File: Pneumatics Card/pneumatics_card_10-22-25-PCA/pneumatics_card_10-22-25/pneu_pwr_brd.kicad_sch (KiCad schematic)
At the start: 40 parts, among them J1 2X1, J2 2X1, J3 2X1, J4 2X1, J5 2X1, J6 2X1, Q1 BSS138, Q2 BSS138, Q3 FQP30N06L, Q4 FQP30N06L, Q5 FQP30N06L, Q6 FQP30N06L, Q7 IRF4905SPbF, U1 L7805, U2 LD1117V33, U3 PCA9685

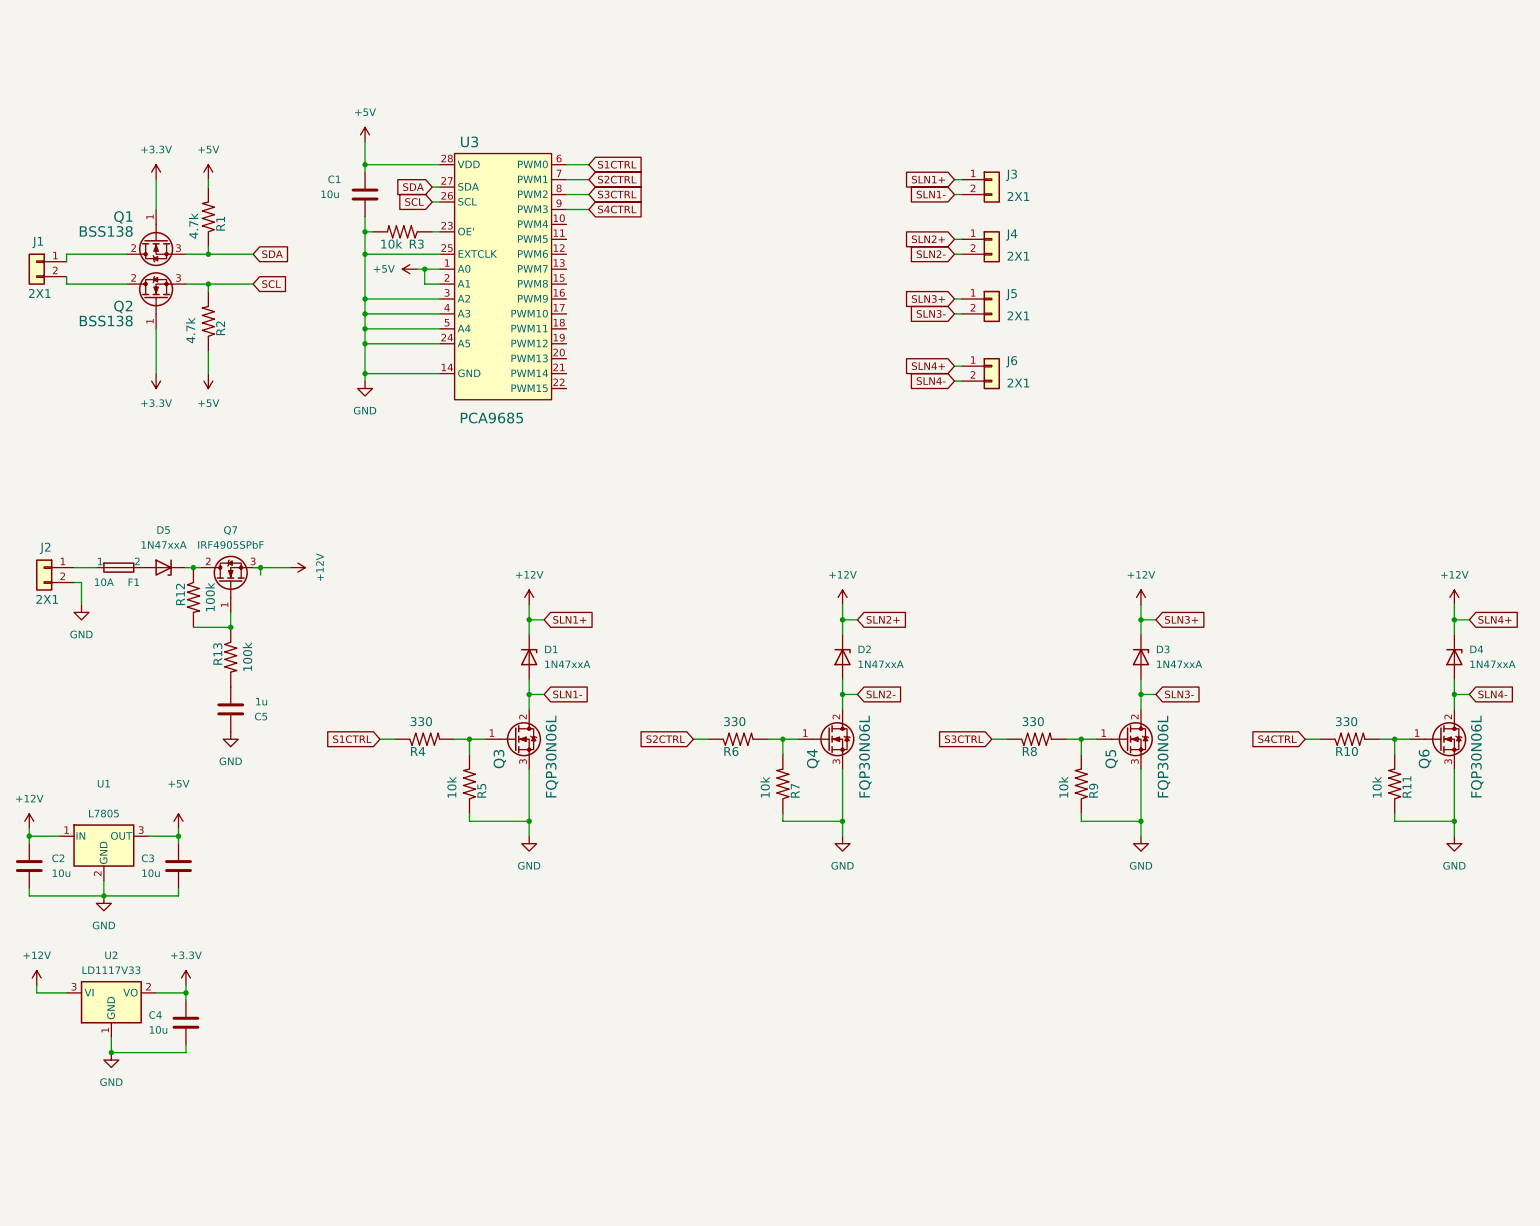
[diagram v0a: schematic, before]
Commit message: added inrush protection to old pneumatics board
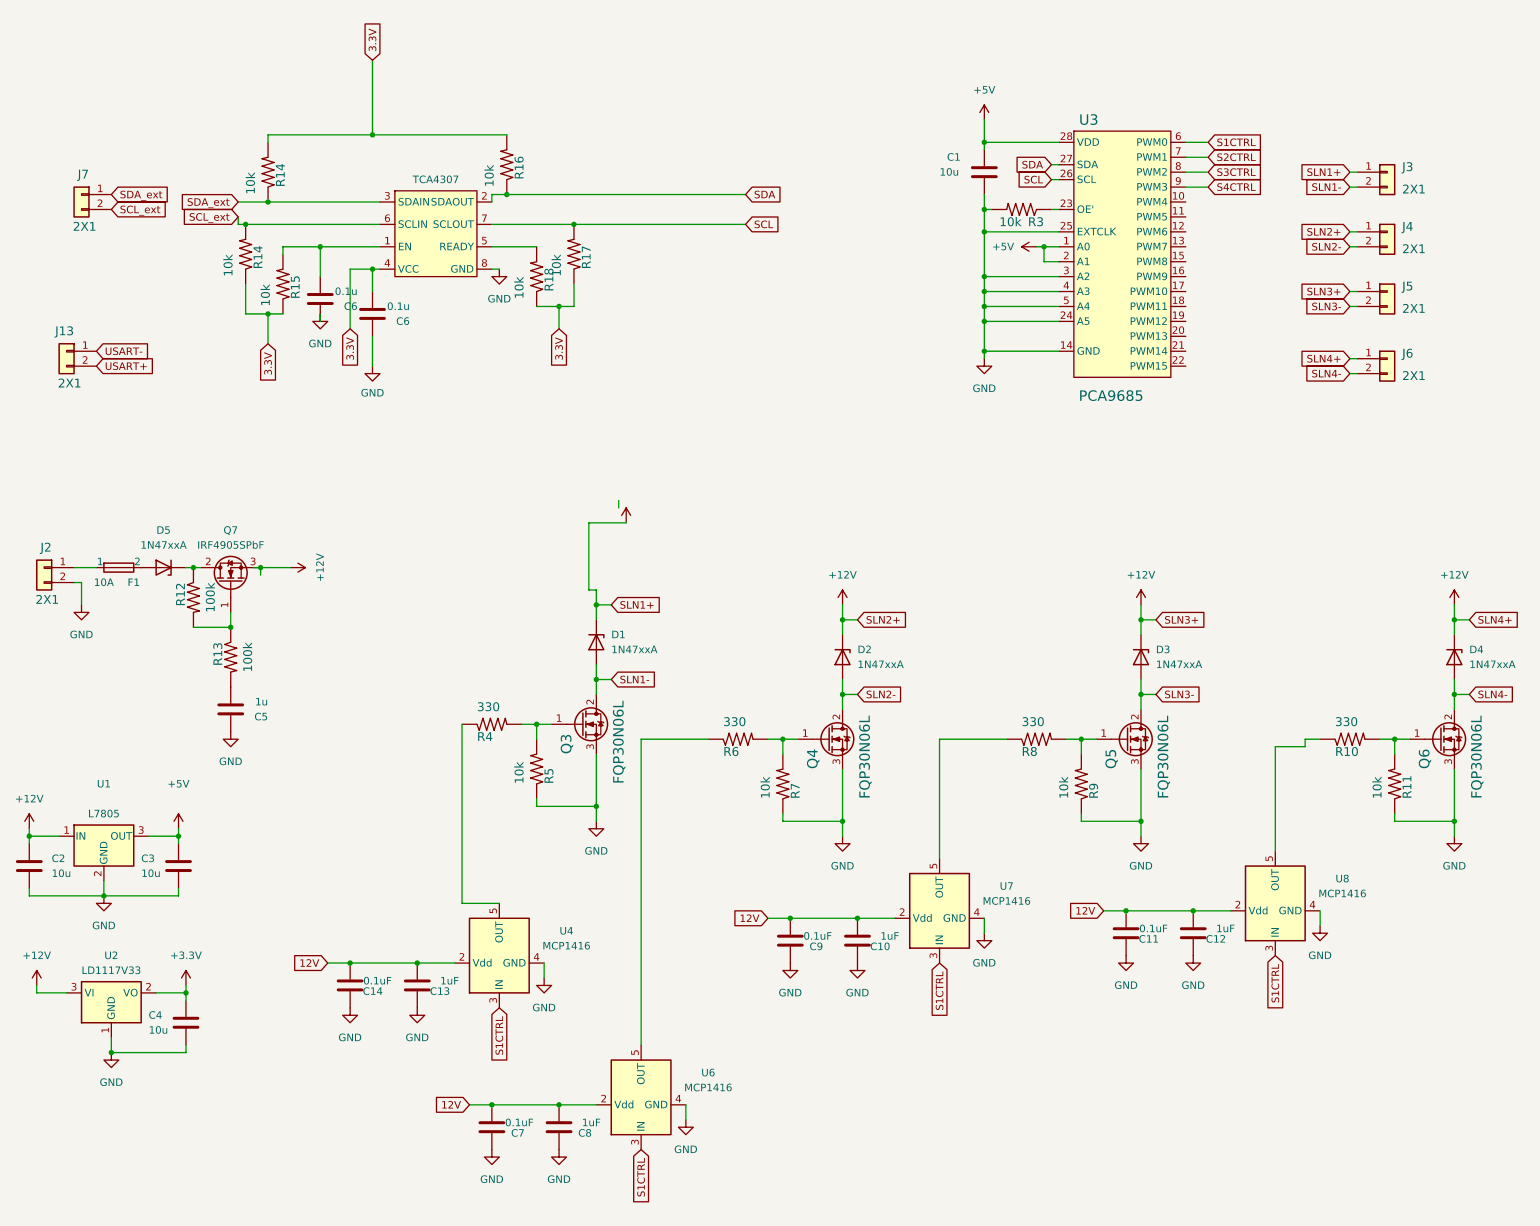
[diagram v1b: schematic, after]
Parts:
- removed J1: 2X1, Connector_JST:JST_PH_B2B-PH-K_1x02_P2.00mm_Vertical, symbol Connector_Generic:Conn_01x02
- removed Q1, Q2: BSS138, Package_TO_SOT_SMD:SOT-23_Handsoldering, symbol Transistor_FET:IRLZ34N
- removed R1, R2: 4.7k, Resistor_SMD:R_0805_2012Metric_Pad1.20x1.40mm_HandSolder, symbol PowerboardRev5-eagle-import:R-US_R0805
- added C10, C12, C13, C8: 1uF, Capacitor_SMD:C_0402_1005Metric, symbol Device:C
- added C11, C14, C7, C9: 0.1uF, Capacitor_SMD:C_0402_1005Metric, symbol Device:C
- added C6 (x2): 0.1u, Capacitor_SMD:C_0603_1608Metric, symbol Device:C
- added J13, J7: 2X1, Connector_JST:JST_PH_B2B-PH-K_1x02_P2.00mm_Vertical, symbol Connector_Generic:Conn_01x02
- added R14 (x2), R15, R16, R17, R18: 10k, Resistor_SMD:R_0603_1608Metric, symbol PowerboardRev5-eagle-import:R-US_R0805
- added U4, U6, U7, U8: MCP1416, Package_TO_SOT_SMD:SOT-23-5, symbol Driver_FET:MCP1416
- added U5: TCA4307, custom_components:SOIC8_DGK_TEX, symbol I2C_Buffer:T_1
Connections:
- net GND: now also C10.1, C11.1, C12.1, C13.1, C14.1, C6.1, C6.1, C7.1, C8.1, C9.1, U4.4 (GND), U5.8 (GND), U6.4 (GND), U7.4 (GND), U8.4 (GND)
- net S1CTRL: now also U4.3 (IN), U6.3 (IN), U7.3 (IN), U8.3 (IN); no longer R4.1
- net S2CTRL: no longer R6.1
- net S3CTRL: no longer R8.1
- net S4CTRL: no longer R10.1
- net SCL: now also R17.2, U5.7 (SCLOUT)
- net SDA: now also R16.1, U5.2 (SDAOUT)
- new net: R4.1, U4.5 (OUT)
- new net: R8.1, U7.5 (OUT)
- new net: R18.2, U5.5 (READY)
- new net: C6.2, R15.2, U5.1 (EN)
- new net: R10.1, U8.5 (OUT)
- new net: R6.1, U6.5 (OUT)
- new net 12V: C10.2, C11.2, C12.2, C13.2, C14.2, C7.2, C8.2, C9.2, U4.2 (Vdd), U6.2 (Vdd), U7.2 (Vdd), U8.2 (Vdd)
- new net 3.3V: C6.2, R14.1, R14.2, R15.1, R16.2, R17.1, R18.1, U5.4 (VCC)
- new net SCL_ext: J7.2 (Pin_2), R14.2, U5.6 (SCLIN)
- new net SDA_ext: J7.1 (Pin_1), R14.1, U5.3 (SDAIN)
- new net USART+: J13.2 (Pin_2)
- new net USART-: J13.1 (Pin_1)
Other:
- moved on the sheet: C1, D1, J3, J4, J5, J6, Q3, R3, R4, R5, U3

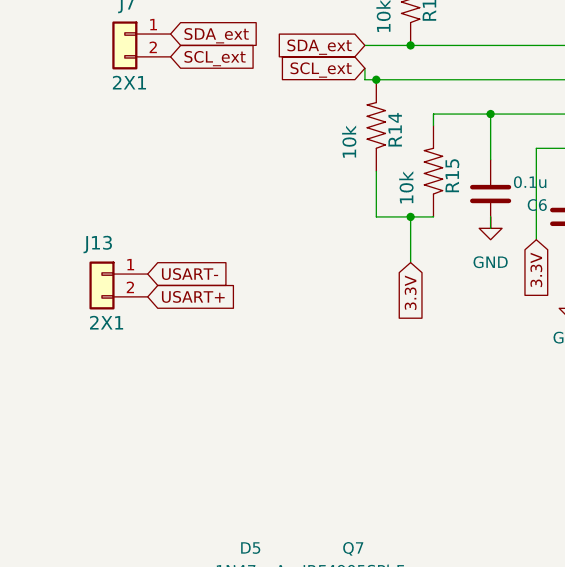
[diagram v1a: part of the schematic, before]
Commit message: fixed footprint for old pneumatics card
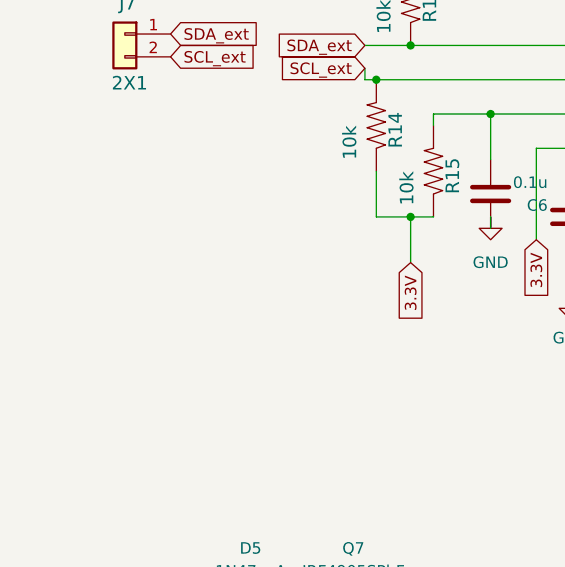
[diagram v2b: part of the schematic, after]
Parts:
- removed J13: 2X1, Connector_JST:JST_PH_B2B-PH-K_1x02_P2.00mm_Vertical, symbol Connector_Generic:Conn_01x02
- U5: footprint custom_components:SOIC8_DGK_TEX -> TCA4307:SOP65P490X110-8N
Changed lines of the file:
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@@
 		)
 	)
-	(global_label "USART-"
-		(shape input)
-		(at 35.56 58.42 0)
-		(fields_autoplaced yes)
-		(effects
-			(font
-				(size 1.27 1.27)
-			)
-			(justify left)
-		)
-		(property "Intersheetrefs" "${INTERSHEET_REFS}"
-			(at 45.9838 58.42 0)
-			(effects
-				(font
-					(size 1.27 1.27)
-				)
-				(justify left)
-				(hide yes)
-			)
-		)
-	)
 	(global_label "SLN1+"
 		(shape input)
@@
 		)
 	)
-	(global_label "USART+"
-		(shape input)
-		(at 35.56 60.96 0)
-		(fields_autoplaced yes)
-		(effects
-			(font
-				(size 1.27 1.27)
-			)
-			(justify left)
-		)
-		(property "Intersheetrefs" "${INTERSHEET_REFS}"
-			(at 45.9838 60.96 0)
-			(effects
-				(font
-					(size 1.27 1.27)
-				)
-				(justify left)
-				(hide yes)
-			)
-		)
-	)
 	(global_label "SLN3+"
 		(shape input)
@@
 	)
 	(symbol
-		(lib_id "Connector_Generic:Conn_01x02")
-		(at 30.48 58.42 0)
-		(mirror y)
-		(unit 1)
-		(exclude_from_sim no)
-		(in_bom yes)
-		(on_board yes)
-		(dnp no)
-		(property "Reference" "J13"
-			(at 31.75 55.88 0)
-			(effects
-				(font
-					(size 1.4986 1.4986)
-				)
-				(justify left bottom)
-			)
-		)
-		(property "Value" "2X1"
-			(at 33.02 64.77 0)
-			(effects
-				(font
-					(size 1.4986 1.4986)
-				)
-				(justify left bottom)
-			)
-		)
-		(property "Footprint" "Connector_JST:JST_PH_B2B-PH-K_1x02_P2.00mm_Vertical"
-			(at 30.48 58.42 0)
-			(effects
-				(font
-					(size 1.27 1.27)
-				)
-				(hide yes)
-			)
-		)
-		(property "Datasheet" "~"
-			(at 30.48 58.42 0)
-			(effects
-				(font
-					(size 1.27 1.27)
-				)
-				(hide yes)
-			)
-		)
-		(property "Description" ""
-			(at 30.48 58.42 0)
-			(effects
-				(font
-					(size 1.27 1.27)
-				)
-			)
-		)
-		(pin "1"
-		)
-		(pin "2"
-		)
-		(instances
-			(project "pneu_pwr_brd"
-				(path "/c299c6f2-212e-472c-8577-e7ed124513dd"
-					(reference "J13")
-					(unit 1)
-				)
-			)
-		)
-	)
-	(symbol
 		(lib_id "PowerboardRev5-eagle-import:R-US_R0805")
 		(at 67.31 46.99 270)
@@
 			)
 		)
-		(property "Footprint" "custom_components:SOIC8_DGK_TEX"
+		(property "Footprint" "TCA4307:SOP65P490X110-8N"
 			(at 96.52 35.56 0)
 			(effects

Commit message: tesitng
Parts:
- renumbered R15 to R155
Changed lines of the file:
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@@
 		(on_board yes)
 		(dnp no)
-		(property "Reference" "R15"
+		(property "Reference" "R155"
 			(at 68.58 49.53 0)
 			(effects
@@
 			(project "pneu_pwr_brd"
 				(path "/c299c6f2-212e-472c-8577-e7ed124513dd"
-					(reference "R15")
+					(reference "R155")
 					(unit 1)
 				)

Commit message: testing
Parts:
- renumbered R155 to R15
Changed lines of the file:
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@@
 		(on_board yes)
 		(dnp no)
-		(property "Reference" "R155"
+		(property "Reference" "R15"
 			(at 68.58 49.53 0)
 			(effects
@@
 			(project "pneu_pwr_brd"
 				(path "/c299c6f2-212e-472c-8577-e7ed124513dd"
-					(reference "R155")
+					(reference "R15")
 					(unit 1)
 				)
